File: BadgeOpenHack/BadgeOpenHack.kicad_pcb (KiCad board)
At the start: 2 copper layers, 49.8 x 49.8 mm, 25 parts, among them J1 Conn_01x04_Male, J2 USB_B_Micro, U1 ATSAMD11C14A-SS

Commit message: pcb propuesta
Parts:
- removed D8: MBR120, Diode_THT:D_DO-201AD_P15.24mm_Horizontal
- removed the G*** at (150.7, 103.8)
- added G***: LOGO, Aesthetics:openhack_negativo, B.Cu at (145.5, 108.6)
- added Ref** (x2): Val**, seguridad-03, F.Cu at (150.2, 99.7)
- moved J1 25.8 mm to (161.4, 83.0), turned to 225 degrees
- moved R7 24.4 mm to (150.0, 98.2)
- moved J2 22.5 mm to (161.6, 109.8), turned to 225 degrees
- moved D7 20.7 mm to (150.0, 102.8)
- moved G*** 18.4 mm to (142.2, 96.2)
- moved G*** 15.7 mm to (157.6, 99.8)
- moved R2 14.7 mm to (136.3, 91.6)
- moved R3 14.4 mm to (164.3, 91.7)
- moved R8 11.3 mm to (165.5, 98.9)
- moved D9 11.2 mm to (165.4, 102.3)
- moved D6 11.1 mm to (135.2, 102.1)
- moved R6 10.4 mm to (135.2, 105.6)
- moved D2 9.83 mm to (136.1, 94.8)
- moved D5 9.27 mm to (141.2, 87.4)
- moved D3 9.08 mm to (164.5, 94.9)
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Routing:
- added copper zone on B.Cu, net GND
- added copper zone on F.Cu, net GND
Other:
- board size 49.8 x 49.8 mm -> 38.1 x 48.2 mm

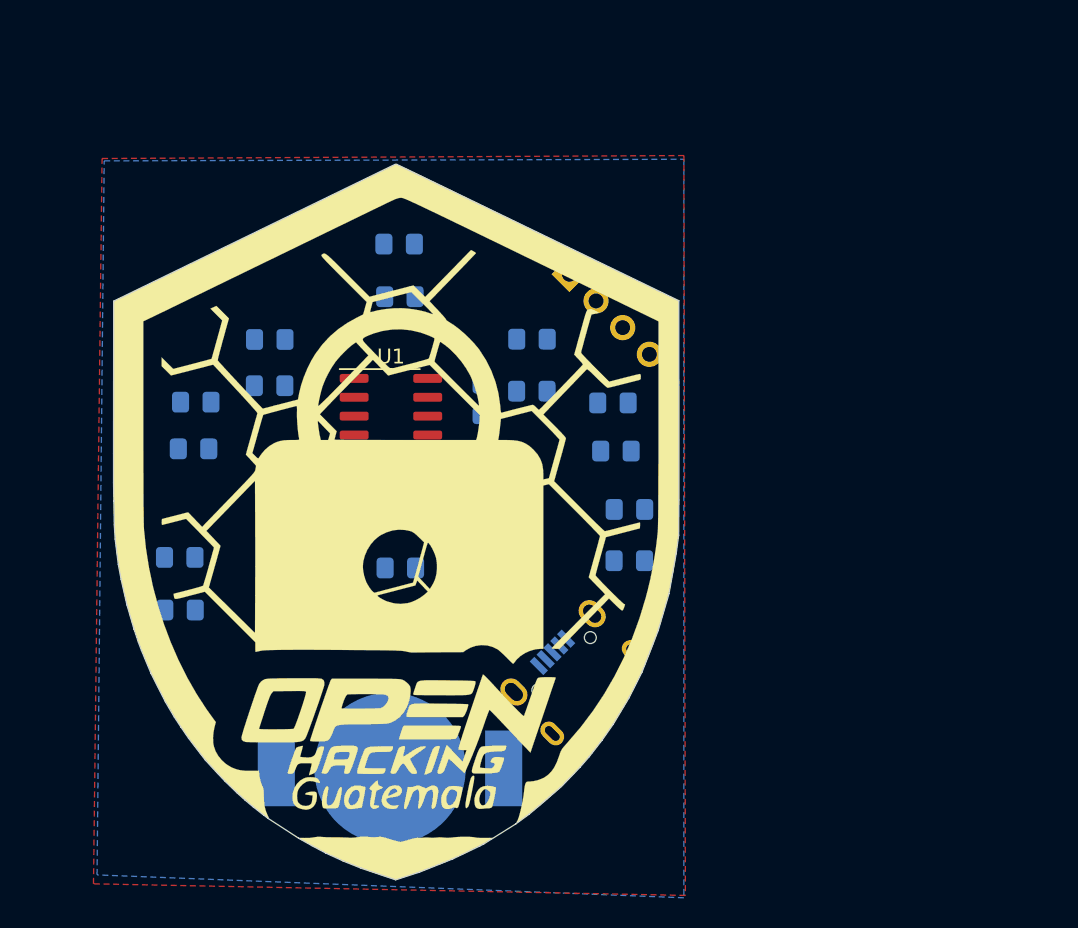
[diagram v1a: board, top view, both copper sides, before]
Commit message: Update schematics change footprints and floorplan
TODO:
- Change SAMD11 to LEDs pins
- Add reset button
- Add action button
- add hole for lanyard
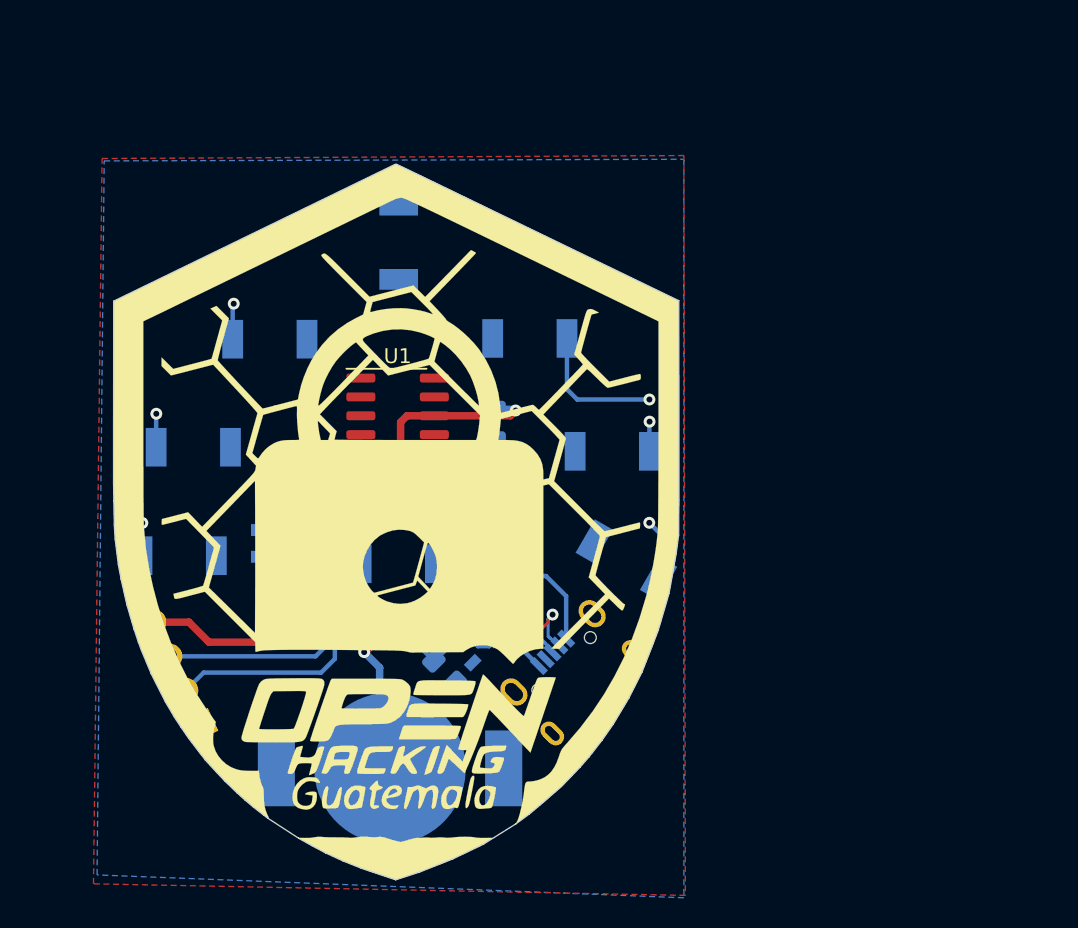
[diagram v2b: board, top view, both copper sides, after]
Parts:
- removed R1, R2, R3, R4, R5, R6, R7, R8: 180, Resistor_SMD:R_0805_2012Metric_Pad1.15x1.40mm_HandSolder
- added C2: 10uF, Capacitor_SMD:C_0805_2012Metric_Pad1.15x1.40mm_HandSolder, B.Cu at (157.1, 105.7)
- added C3: 10uF, Capacitor_SMD:C_0805_2012Metric_Pad1.15x1.40mm_HandSolder, B.Cu at (153.0, 109.8)
- added D8: R_LED, BadgeOpenHack:LYT77K-K2M1-NoHole, B.Cu at (149.9, 102.5)
- added G***: LOGO, Aesthetics:electronic_cats_logo_4x3, B.Cu at (180.0, 101.0)
- added RN1: R_Pack04, Resistor_SMD:R_Array_Convex_4x0603, B.Cu at (141.4, 101.1)
- added RN2: R_Pack04, Resistor_SMD:R_Array_Convex_4x0603, B.Cu at (157.9, 101.2)
- added U2: AP2112K-3.3, Package_TO_SOT_SMD:SOT-23-5, B.Cu at (155.0, 107.7)
- D1, D2, D3, D4, D5, D6, D7: value LED -> R_LED; footprint LED_SMD:LED_0805_2012Metric_Pad1.15x1.40mm_HandSolder -> BadgeOpenHack:LYT77K-K2M1-NoHole
- D9: value LED -> MBR120; footprint LED_SMD:LED_0805_2012Metric_Pad1.15x1.40mm_HandSolder -> Diode_SMD:D_SOD-123F
- moved G*** 46.0 mm to (189.5, 95.5)
- moved J1 39.1 mm to (136.7, 113.3), turned to 25 degrees
- moved D6 30.0 mm to (164.3, 95.0)
- moved D1 25.7 mm to (135.2, 102.0)
- moved D3 24.5 mm to (141.2, 87.4), turned to 180 degrees
- moved G*** 17.9 mm to (141.2, 107.2)
- moved D5 17.5 mm to (158.8, 87.3)
- moved D7 15.2 mm to (165.2, 102.2), turned to 330 degrees
- moved D9 12.9 mm to (153.0, 105.8), turned to 225 degrees
- moved D4 11.1 mm to (149.9, 80.9), turned to 270 degrees
- moved G*** 8.74 mm to (149.9, 92.0)
- moved C1 1.84 mm to (156.4, 93.1)
- moved U1 0.45 mm to (149.8, 93.8)
- moved D2 0.11 mm to (136.1, 94.7), turned to 180 degrees
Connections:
- D9 pad 1: Net-(D9-Pad1) -> +3V3
- D9 pad 2: /SWDIO -> Net-(C3-Pad1)
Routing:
- net +3V3: track 0.00 -> 65.7 mm, vias 0 -> 6
- net /SWDIO: track 0.00 -> 40.0 mm, vias 0 -> 1
- net /SWCLK: track 0.00 -> 23.7 mm, vias 0 -> 1
- net /D-: track 0.00 -> 21.3 mm, vias 0 -> 1
- net /D+: track 0.00 -> 20.9 mm, vias 0 -> 1
- net VCC: track 0.00 -> 14.4 mm
- net /D4: track 0.00 -> 9.26 mm, vias 0 -> 1
- net GND: track 0.00 -> 5.85 mm
- net Net-(C3-Pad1): track 0.00 -> 4.81 mm
- net /D6: track 0.00 -> 4.45 mm, vias 0 -> 1
- net Net-(D9-Pad1): track 0.00 -> 4.12 mm
- net /D2: track 0.00 -> 2.42 mm, vias 0 -> 1
- net /D1: track 0.00 -> 2.26 mm, vias 0 -> 1
- net /D0: track 0.00 -> 2.21 mm, vias 0 -> 1
- net /D5: track 0.00 -> 2.00 mm, vias 0 -> 1
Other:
- net class Default: clearance 0.2 -> 0.1
- rule trace_clearance: 0.2 -> 0.1

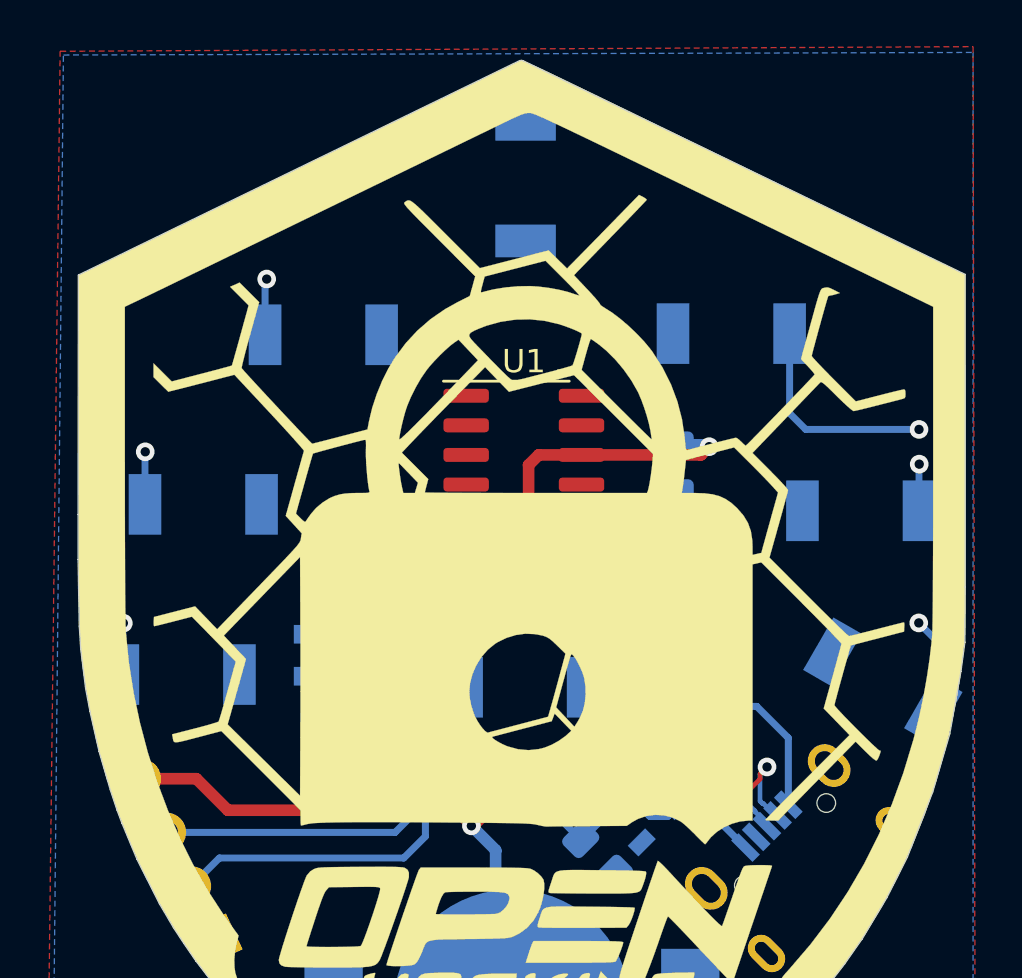
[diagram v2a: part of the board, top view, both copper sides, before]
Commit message: Update LED arrange almost route
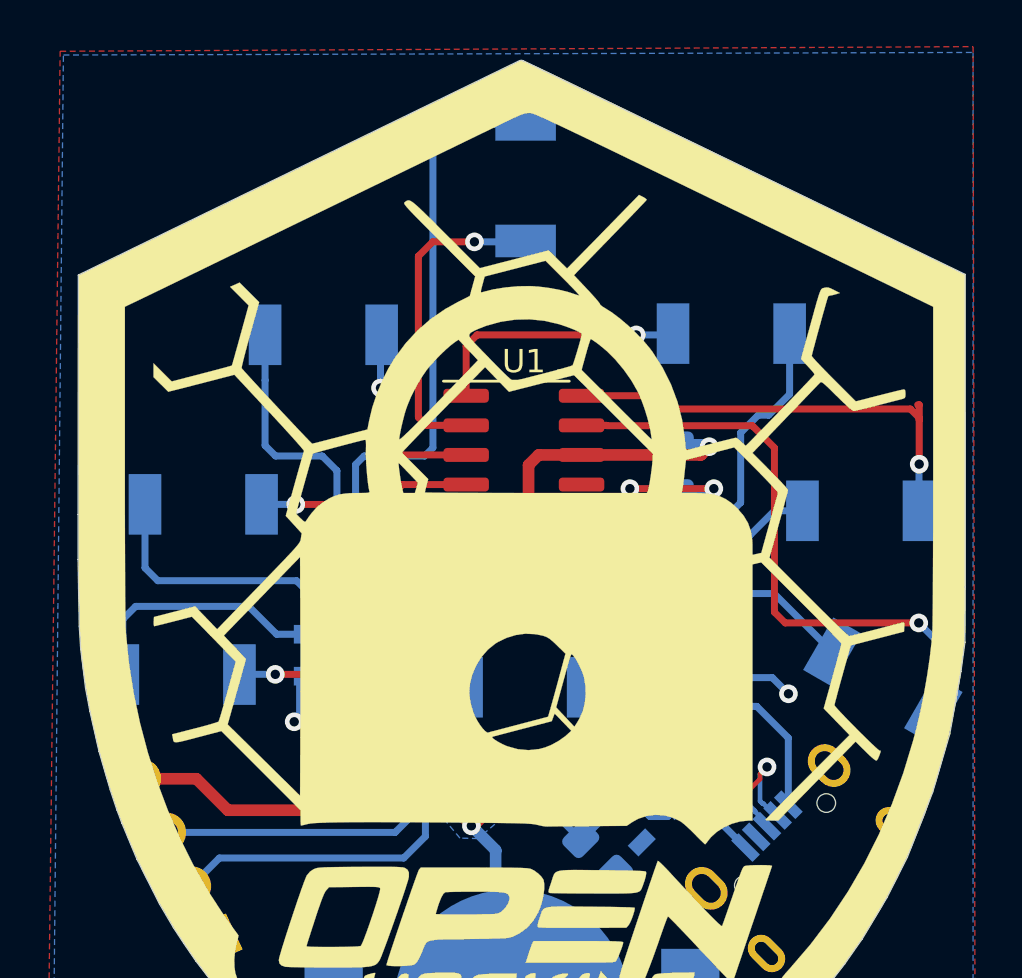
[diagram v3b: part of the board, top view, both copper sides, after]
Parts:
- turned D1 to 0 degrees
- turned D2 to 0 degrees
- turned D3 to 0 degrees
- turned D5 to 180 degrees
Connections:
- U1 pad 13: /D2 -> /D6
- U1 pad 14: /D3 -> /D5
- U1 pad 2: /D0 -> /D3
- U1 pad 3: /D1 -> /D2
- U1 pad 4: /D5 -> /D1
- U1 pad 5: /D6 -> /D0
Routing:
- net Net-(D4-Pad1): track 0.00 -> 28.1 mm
- net /D6: track 4.45 -> 26.6 mm
- net /D5: track 2.00 -> 19.6 mm
- net Net-(D5-Pad1): track 0.00 -> 15.7 mm
- net Net-(D3-Pad1): track 0.00 -> 15.3 mm
- net GND: track 5.85 -> 20.2 mm, vias 0 -> 8
- net /D3: track 0.00 -> 14.0 mm, vias 0 -> 1
- net /D0: track 2.21 -> 15.9 mm
- net Net-(D2-Pad1): track 0.00 -> 12.1 mm
- net Net-(D1-Pad1): track 0.00 -> 10.7 mm
- net Net-(D6-Pad1): track 0.00 -> 8.74 mm
- net Net-(D7-Pad1): track 0.00 -> 7.30 mm
- net /D1: track 2.26 -> 9.13 mm
- net Net-(D8-Pad1): track 0.00 -> 6.67 mm
- net /D2: track 2.42 -> 8.66 mm
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- added copper zone on B.Cu, net +3V3
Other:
- net class Default: clearance 0.1 -> 0.25
- rule trace_clearance: 0.1 -> 0.25

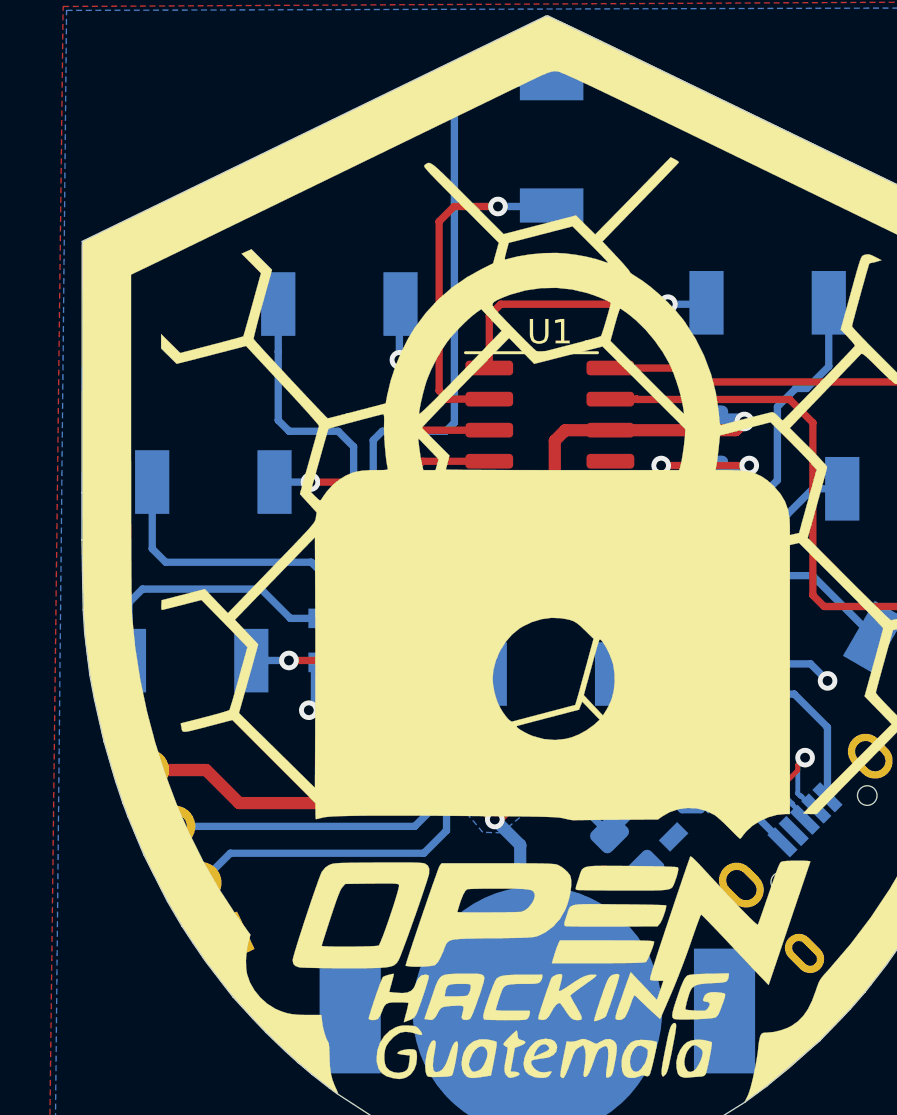
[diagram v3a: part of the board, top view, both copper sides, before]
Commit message: add rst button complete route
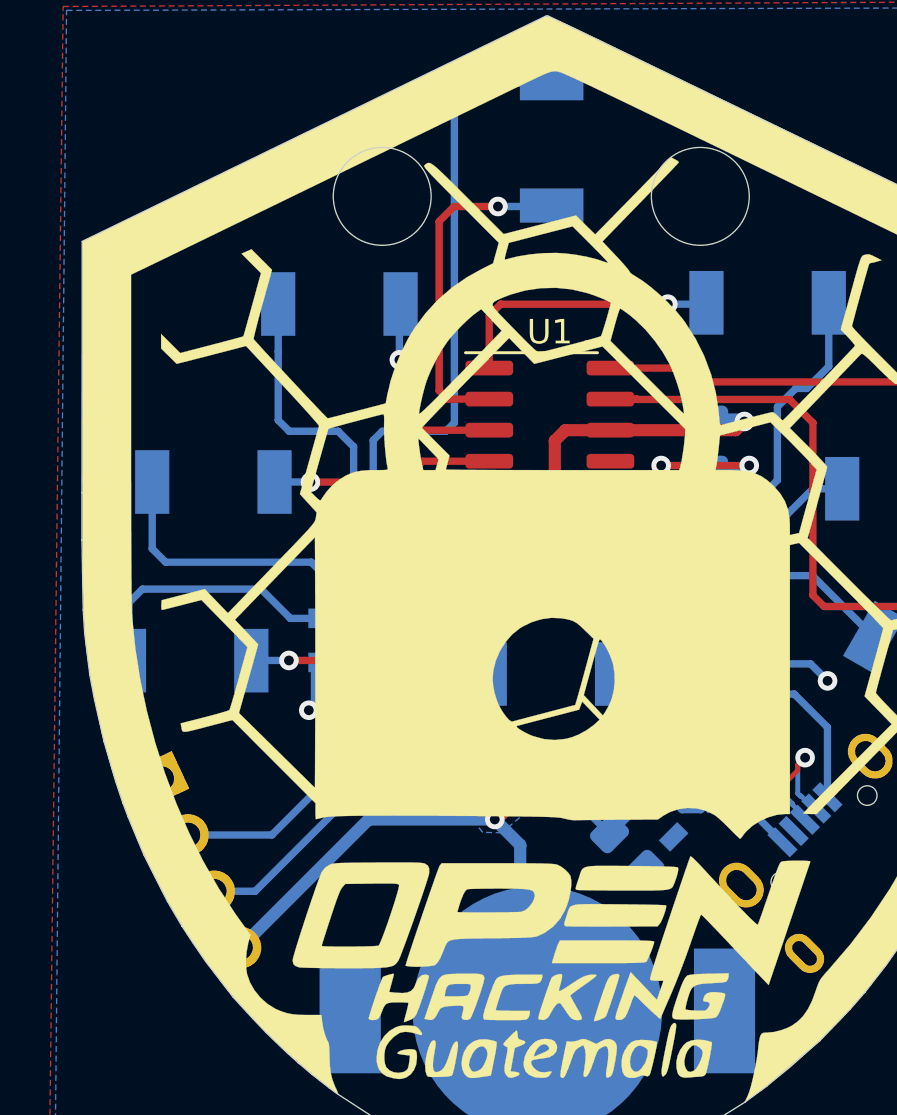
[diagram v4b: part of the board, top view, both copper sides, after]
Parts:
- added REF**: OSHW-Logo2_7.3x6mm_SilkScreen, Symbol:OSHW-Logo2_7.3x6mm_SilkScreen, B.Cu at (134.9, 89.3)
- added SW1: RST, Button_Switch_SMD:SW_SPST_TL3342, B.Cu at (150.0, 96.7)
- moved J1 7.08 mm to (134.0, 106.8), turned to 205 degrees
- moved G*** 3.00 mm to (149.9, 89.0)
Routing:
- net /RST: track 0.00 -> 11.3 mm, vias 0 -> 1
- net +3V3: track 65.7 -> 61.3 mm
- net /SWDIO: track 40.0 -> 36.4 mm
- net GND: track 20.2 -> 22.5 mm, vias 8 -> 9
- net /SWCLK: track 23.7 -> 21.5 mm
- net Net-(D8-Pad1): track 6.67 -> 8.58 mm
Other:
- outline, holes or cut-outs redrawn
- board text added: "V1.0"

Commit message: Fix traces
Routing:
- net /D5: track 19.6 -> 18.9 mm
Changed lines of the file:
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@@
     (thickness 1.6)
     (drawings 58)
-    (tracks 269)
+    (tracks 267)
     (zones 0)
     (modules 27)
@@
   (segment (start 166.8 92.96) (end 166.81 92.95) (width 0.3) (layer B.Cu) (net 12))
   (segment (start 166.8 94.95) (end 166.8 92.96) (width 0.3) (layer B.Cu) (net 12))
-  (segment (start 166.81 90.404) (end 166.742 90.404) (width 0.3) (layer F.Cu) (net 12))
   (segment (start 166.81 91.06) (end 166.81 90.96) (width 0.3) (layer F.Cu) (net 12))
   (segment (start 166.81 92.95) (end 166.81 91.06) (width 0.3) (layer F.Cu) (net 12))
-  (segment (start 166.81 91.06) (end 166.81 90.404) (width 0.3) (layer F.Cu) (net 12))
   (segment (start 166.43499 90.58499) (end 155.53499 90.58499) (width 0.3) (layer F.Cu) (net 12))
   (segment (start 155.53499 90.58499) (end 154.965 90.015) (width 0.3) (layer F.Cu) (net 12))
